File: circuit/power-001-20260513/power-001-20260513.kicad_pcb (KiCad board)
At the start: 2 copper layers, 68.4 x 46.4 mm, 59 parts, among them J1 VIN, J2 +5V_{Line}, J3 Power, J4 Logic, J5 Sub_{Power}, J6 Sub_{Signal}, J7 ICSP_{PIC12F683}, Q1 BSS138, Q2 PMOS, SW1 SW_SPDT, SW2 SW_SPDT, SW3 SW_SPDT, SW4 Locker_SW, U1 OKL-T/6-W12N-C, U2 OKL-T/6-W12N-C, U3 AZ1084-3.3, U4 BP5293-33, U5 PIC12F683-xSN

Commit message: Update 電源基板の配置が苦しい
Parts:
- removed D1: LED, LED_SMD:LED_0603_1608Metric
- removed R16: 330, Resistor_SMD:R_0805_2012Metric
- removed TP1, TP2: TP_{+5V-Line}, TestPoint:TestPoint_Loop_D1.80mm_Drill1.0mm_Beaded
- removed TP3: TP_{+5V}, TestPoint:TestPoint_Loop_D1.80mm_Drill1.0mm_Beaded
- removed TP4: TP_{+3.3V}, TestPoint:TestPoint_Loop_D1.80mm_Drill1.0mm_Beaded
- removed TP5: TP_{GND}, TestPoint:TestPoint_Loop_D1.80mm_Drill1.0mm_Beaded
- removed U4: BP5293-33, @Thrive_footprint_power:BP5293-33
- added C13: 10μ, Capacitor_SMD:C_0805_2012Metric, F.Cu at (144.7, 101.5)
- added U6: LM1117MP-3.3, Package_TO_SOT_SMD:SOT-223-3_TabPin2, B.Cu at (103.7, 88.8)
- C1, Q1: moved to F.Cu
- C11, C12, C2, C3, C4, C7, R10, R11, R13, R18, R19, R5, R7, U2, U3: moved to B.Cu
- C5: value 1000μ -> 10μ; footprint Capacitor_THT:CP_Radial_D10.0mm_P5.00mm -> Capacitor_SMD:C_0805_2012Metric; moved to F.Cu
- J2, J3, J4, J5: footprint Connector_AMASS:AMASS_XT30PW-F_1x02_P2.50mm_Horizontal -> @Thrive_footprint_power:AMASS_XT30PW-F_1x02_P2.50mm_Horizontal
- J7: footprint Connector_PinHeader_2.54mm:PinHeader_1x05_P2.54mm_Vertical -> Connector_PinHeader_1.00mm:PinHeader_1x05_P1.00mm_Vertical
- moved C7 83.2 mm to (68.9, 104.4)
- moved C11 80.6 mm to (75.9, 104.4)
- moved R5 70.9 mm to (63.8, 95.9), turned to 90 degrees
- moved R13 66.3 mm to (72.4, 104.4), turned to 180 degrees
- moved R7 64.5 mm to (74.4, 86.4), turned to 90 degrees
- moved R11 64.1 mm to (76.4, 86.4), turned to -90 degrees
- moved C4 61.7 mm to (93.7, 79.3), turned to -90 degrees
- moved R10 61.5 mm to (78.4, 86.4), turned to -90 degrees
- moved C3 54.6 mm to (100.2, 79.3), turned to -90 degrees
- moved J7 49.3 mm to (115.7, 75.8), turned to 90 degrees
- moved C2 47.5 mm to (106.7, 79.3), turned to -90 degrees
- moved C12 45.3 mm to (117.7, 81.8)
- moved U3 43.3 mm to (108.2, 106.8)
- moved U5 38.5 mm to (117.7, 81.8), turned to 90 degrees
- moved C5 37.4 mm to (135.8, 101.5), turned to 0 degrees
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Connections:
- C5 pad 1: VIN -> VCC
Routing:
- net VIN: track 0.00 -> 49.3 mm, vias 0 -> 4
- net SW_TGL_1: track 0.00 -> 49.3 mm
- net SW_TGL_2: track 0.00 -> 45.3 mm
- net SW_TGL_3: track 0.00 -> 41.4 mm
- net +5V_{Line}: track 0.00 -> 29.4 mm
- net MCLR: track 0.00 -> 11.2 mm, vias 0 -> 1
- net +3.3VA: track 0.00 -> 9.76 mm
- net ICSPCLK: track 0.00 -> 8.01 mm
- net ICSPDAT: track 0.00 -> 6.81 mm, vias 0 -> 1
- net GND: track 0.00 -> 4.31 mm, vias 0 -> 1
- net Net-(U2-Trim): track 0.00 -> 4.01 mm
- net Net-(R11-Pad2): track 0.00 -> 2.00 mm
- net Net-(R10-Pad1): track 0.00 -> 2.00 mm
- net Net-(Q1-G): track 0.00 -> 1.67 mm
- added copper zone on B.Cu, net GND
- added copper zone on F.Cu, net GND
- added copper zone on B.Cu, net Net-(J1-Pin_1)
- added copper zone on F.Cu, net Net-(J1-Pin_1)
- added copper zone on B.Cu, net Net-(SW4-A)
- added copper zone on F.Cu, net Net-(SW4-A)
- added copper zone on B.Cu, net VCC

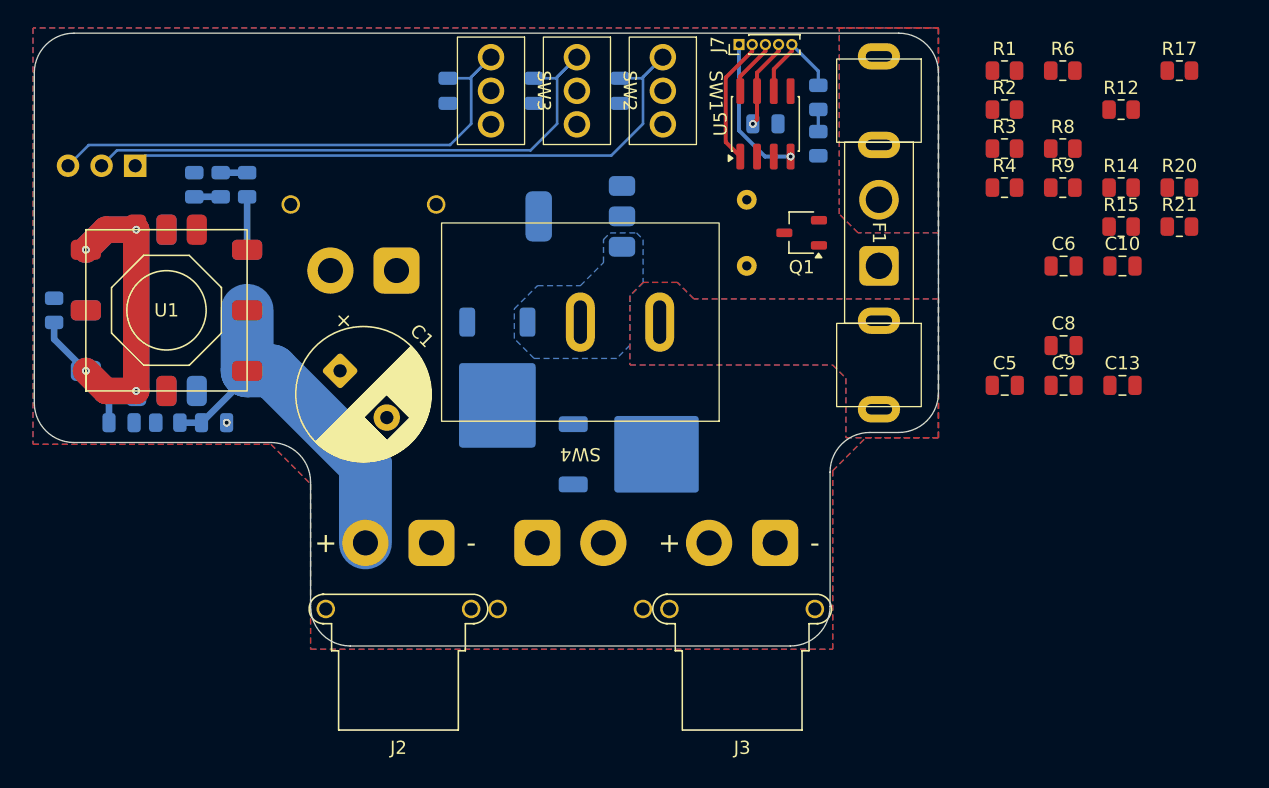
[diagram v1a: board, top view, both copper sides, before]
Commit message: Update 電源基板の回路図とPCBを修正・更新
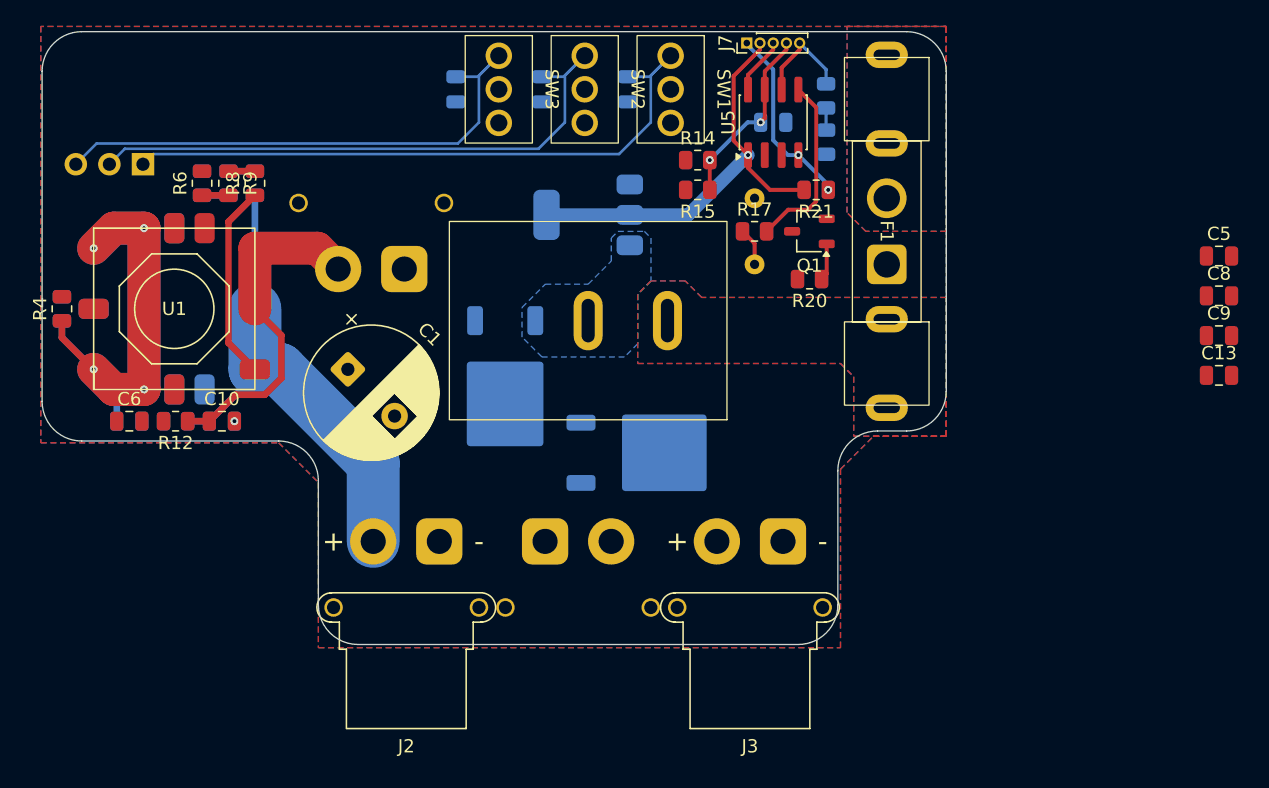
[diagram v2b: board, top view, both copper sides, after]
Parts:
- removed R1, R2, R3: 10k, Resistor_SMD:R_0805_2012Metric
- moved R12 75.3 mm to (73.0, 104.2), turned to 180 degrees
- moved R4 71.9 mm to (64.4, 95.8), turned to 90 degrees
- moved C6 71.6 mm to (69.5, 104.2)
- moved C10 69.1 mm to (76.5, 104.2)
- moved R6 65.7 mm to (75.0, 86.2), turned to 90 degrees
- moved R9 63.1 mm to (77.0, 86.2), turned to -90 degrees
- moved R8 61.2 mm to (79.0, 86.2), turned to 90 degrees
- moved R17 34.4 mm to (116.8, 89.9)
- moved R15 32.1 mm to (112.5, 86.8), turned to 180 degrees
- moved R14 32.1 mm to (112.5, 84.5)
- moved R20 28.8 mm to (121.0, 93.5), turned to 180 degrees
- moved R21 27.6 mm to (121.5, 86.8), turned to 180 degrees
- moved C5 18.9 mm to (152.0, 91.8)
- moved C8 12.3 mm to (152.0, 94.8)
- moved C9 12.3 mm to (152.0, 97.8)
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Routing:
- net +5V: track 0.00 -> 26.0 mm
- net +3.3VA: track 9.76 -> 32.8 mm, vias 0 -> 1
- net Net-(U1-Trim): track 0.00 -> 14.8 mm
- net Prot-Buzzer: track 0.00 -> 13.7 mm
- net ICSPDAT: track 6.81 -> 14.6 mm, vias 1 -> 2
- net VIN: track 49.3 -> 54.0 mm
- net MCLR: track 11.2 -> 14.2 mm, vias 1 -> 2
- net Net-(BZ1-+): track 0.00 -> 2.88 mm
- net Net-(Q1-D): track 0.00 -> 2.82 mm
- net Net-(R8-Pad2): track 0.00 -> 2.00 mm
- net Net-(R6-Pad1): track 0.00 -> 2.00 mm

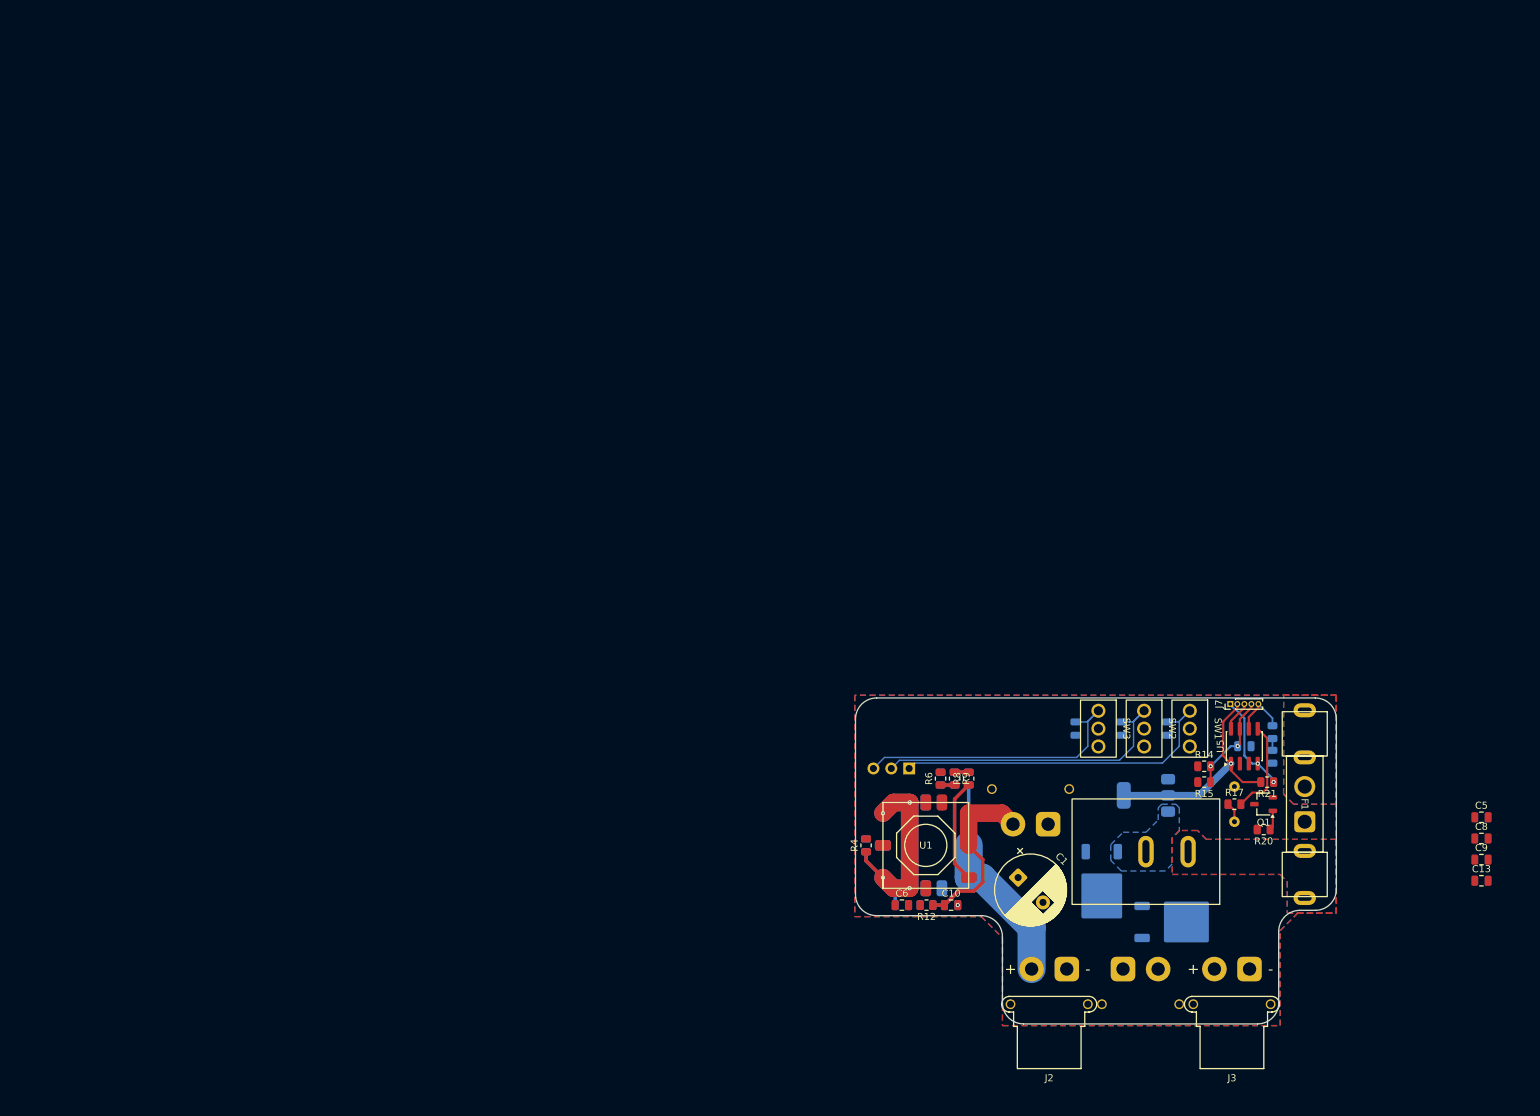
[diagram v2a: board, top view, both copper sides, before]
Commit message: Update 電源基板のチップ部品の配置を一度考え直すために削除
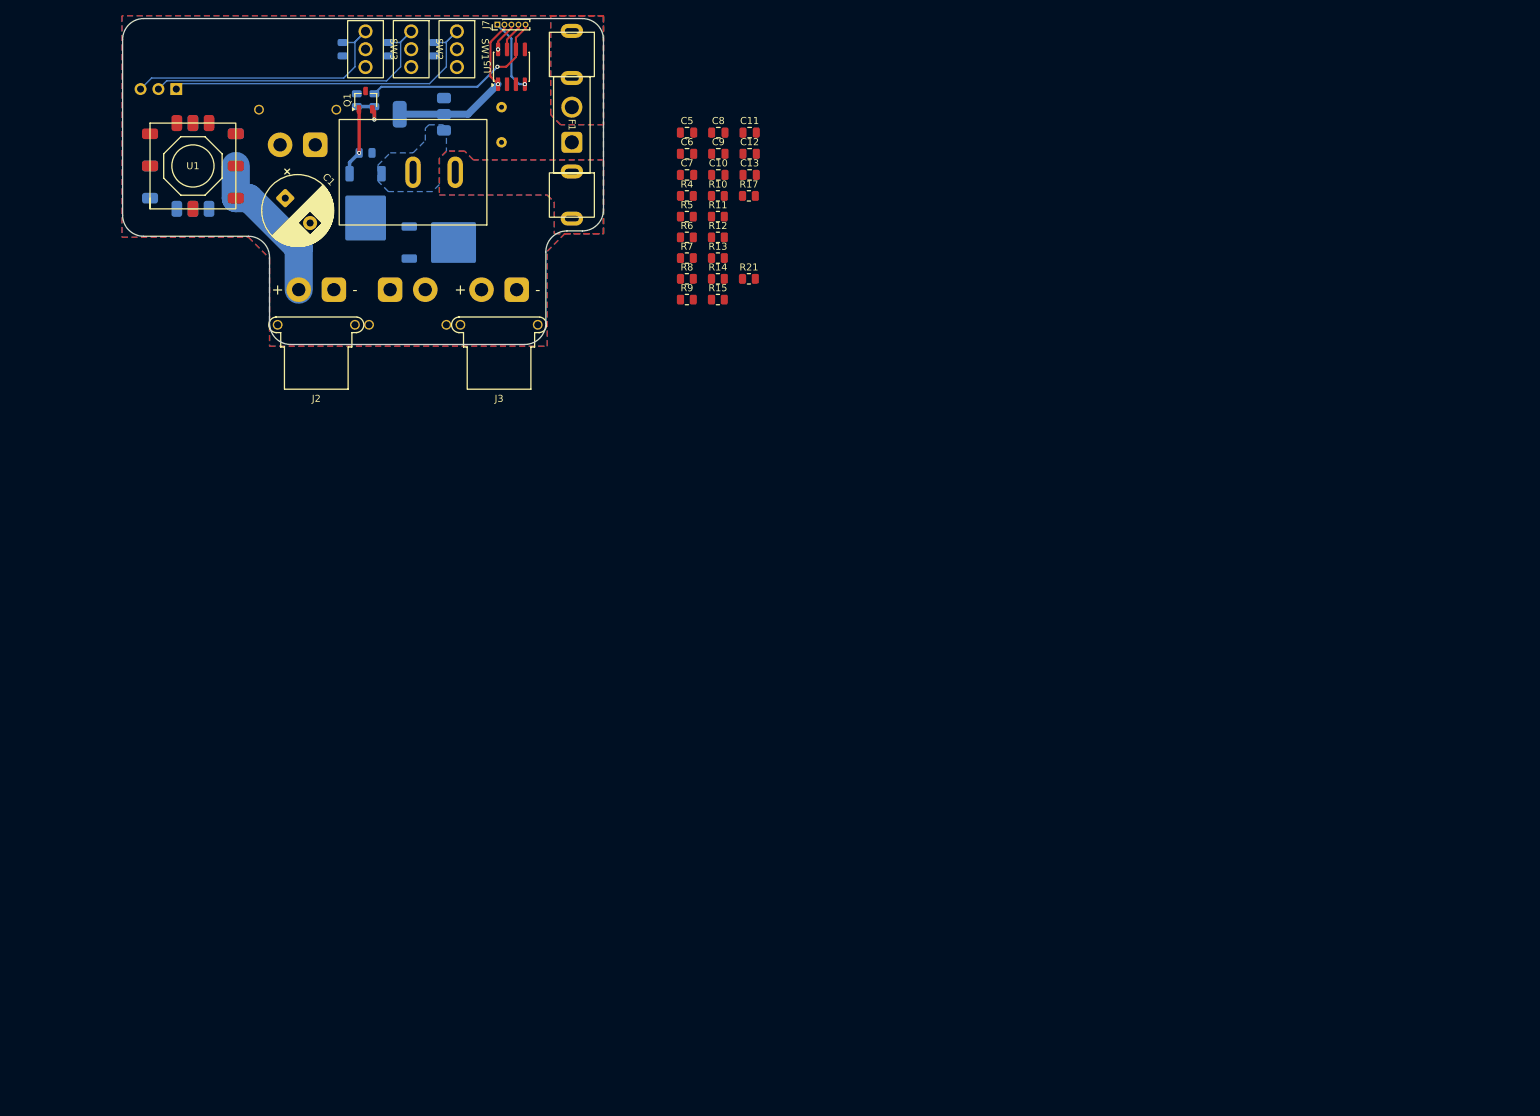
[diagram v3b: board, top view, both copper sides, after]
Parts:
- C11, C12, C7, R10, R11, R13, R5, R7: moved to F.Cu
- R20: moved to B.Cu
- moved Q1 162.3 mm to (-6.75, -10.2), turned to 90 degrees
- moved R19 160.3 mm to (-8.00, -10.2), turned to -90 degrees
- moved R20 160.0 mm to (-6.75, -2.75), turned to 0 degrees
- moved R18 156.2 mm to (-5.50, -10.2)
- moved C5 149.2 mm to (39.0, -5.64)
- moved C8 147.9 mm to (43.4, -5.64)
- moved C9 147.9 mm to (43.4, -2.63)
- moved C13 144.6 mm to (47.9, 0.38)
- moved Q2 142.4 mm to (-6.75, 5.25)
- moved BZ1 142.2 mm to (12.6, -6.76)
- moved C1 142.2 mm to (-18.2, 3.69)
- moved C2 142.2 mm to (2.99, -17.5)
- moved C3 142.2 mm to (-3.51, -17.5)
- moved C4 142.2 mm to (-10.0, -17.5)
- moved F1 142.2 mm to (22.6, -6.76)
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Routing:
- net VIN: track 54.0 -> 0.00 mm, vias 4 -> 0
- net +5V: track 26.0 -> 0.00 mm
- net ICSPCLK: track 8.01 -> 27.5 mm, vias 0 -> 1
- net Net-(U1-Trim): track 14.8 -> 0.00 mm
- net Prot-Buzzer: track 13.7 -> 0.00 mm
- net ICSPDAT: track 14.6 -> 4.20 mm, vias 2 -> 0
- net +3.3VA: track 32.8 -> 25.5 mm
- net +5V_{Line}: track 29.4 -> 22.4 mm
- net Net-(Q1-D): track 2.82 -> 9.73 mm, vias 0 -> 1
- net Net-(Q1-G): track 1.67 -> 5.90 mm, vias 0 -> 1
- net Net-(U2-Trim): track 4.01 -> 0.00 mm
- net MCLR: track 14.2 -> 10.6 mm, vias 2 -> 1
- net Net-(BZ1-+): track 2.88 -> 0.00 mm
- net Net-(R8-Pad2): track 2.00 -> 0.00 mm
- net Net-(R6-Pad1): track 2.00 -> 0.00 mm
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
